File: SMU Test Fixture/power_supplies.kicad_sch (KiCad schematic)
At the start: 60 parts, among them J13 Hot_Spade, J14 Power Outputs, J15 Neutral_Spade, Q1 IRLR6225TRPBF, Q2 NTD3055-150T4G, Q3 MMBT3906, T1 VPP28-1060, U10 LT3045, U11 LT1086-12, U12 LT3094, U13 LTC2966CSWPBF, U9 LT1086-5.0

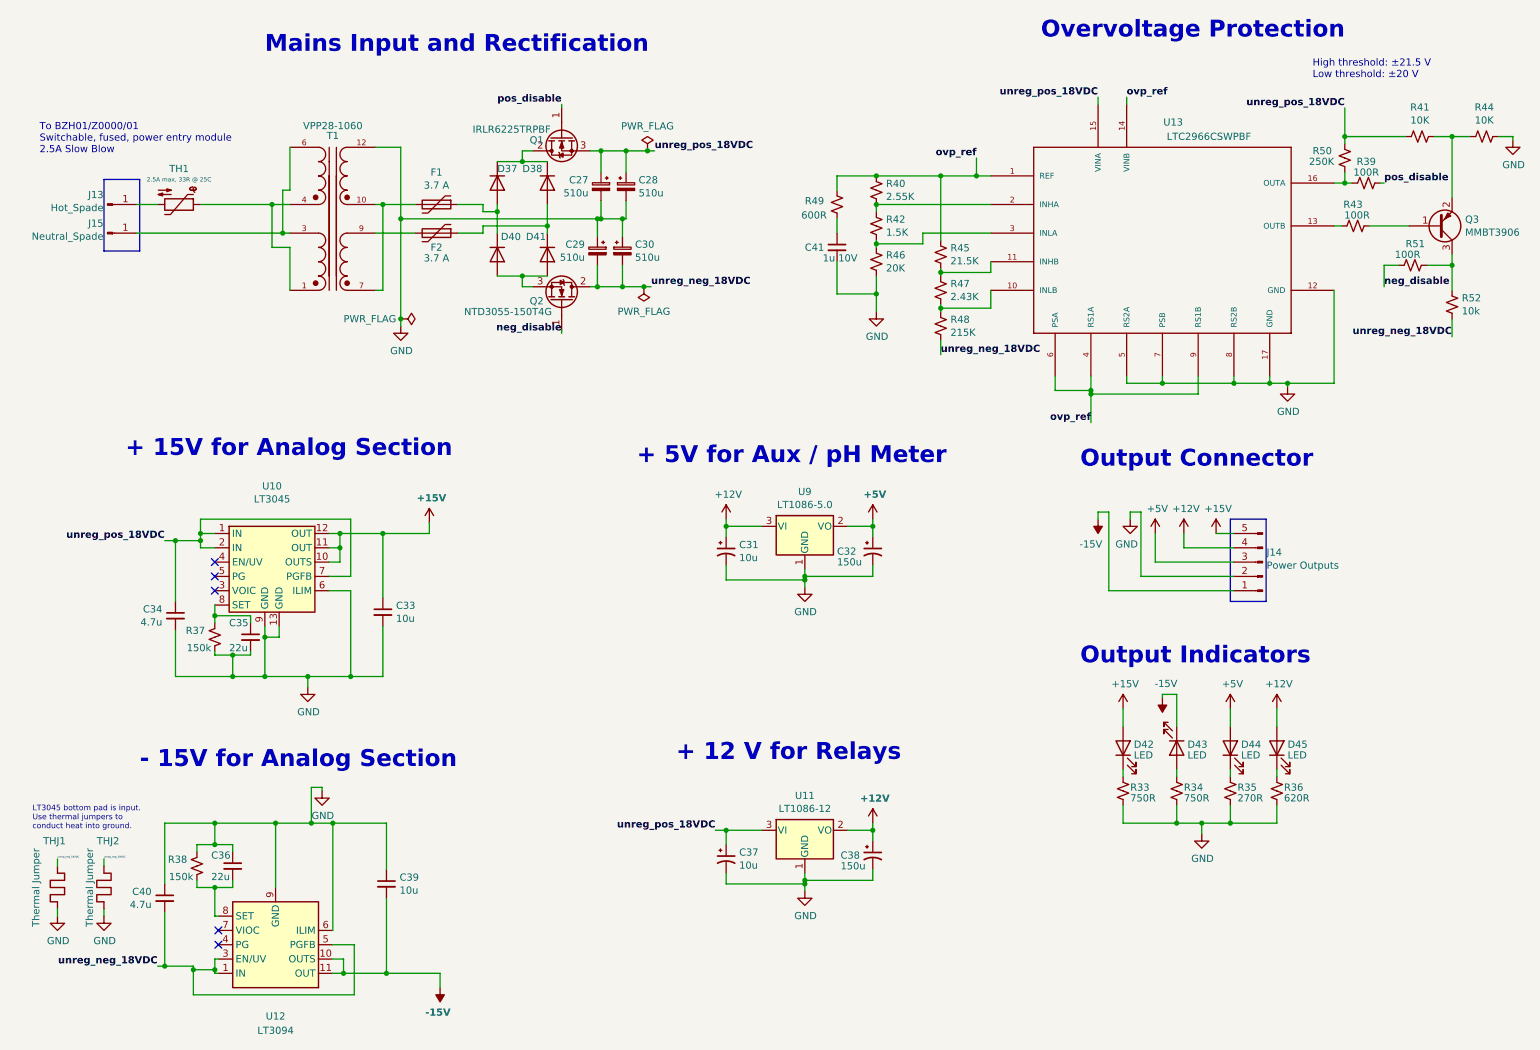
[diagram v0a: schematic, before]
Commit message: Fix grid nightmare. Begin adding bypass caps for a.switches
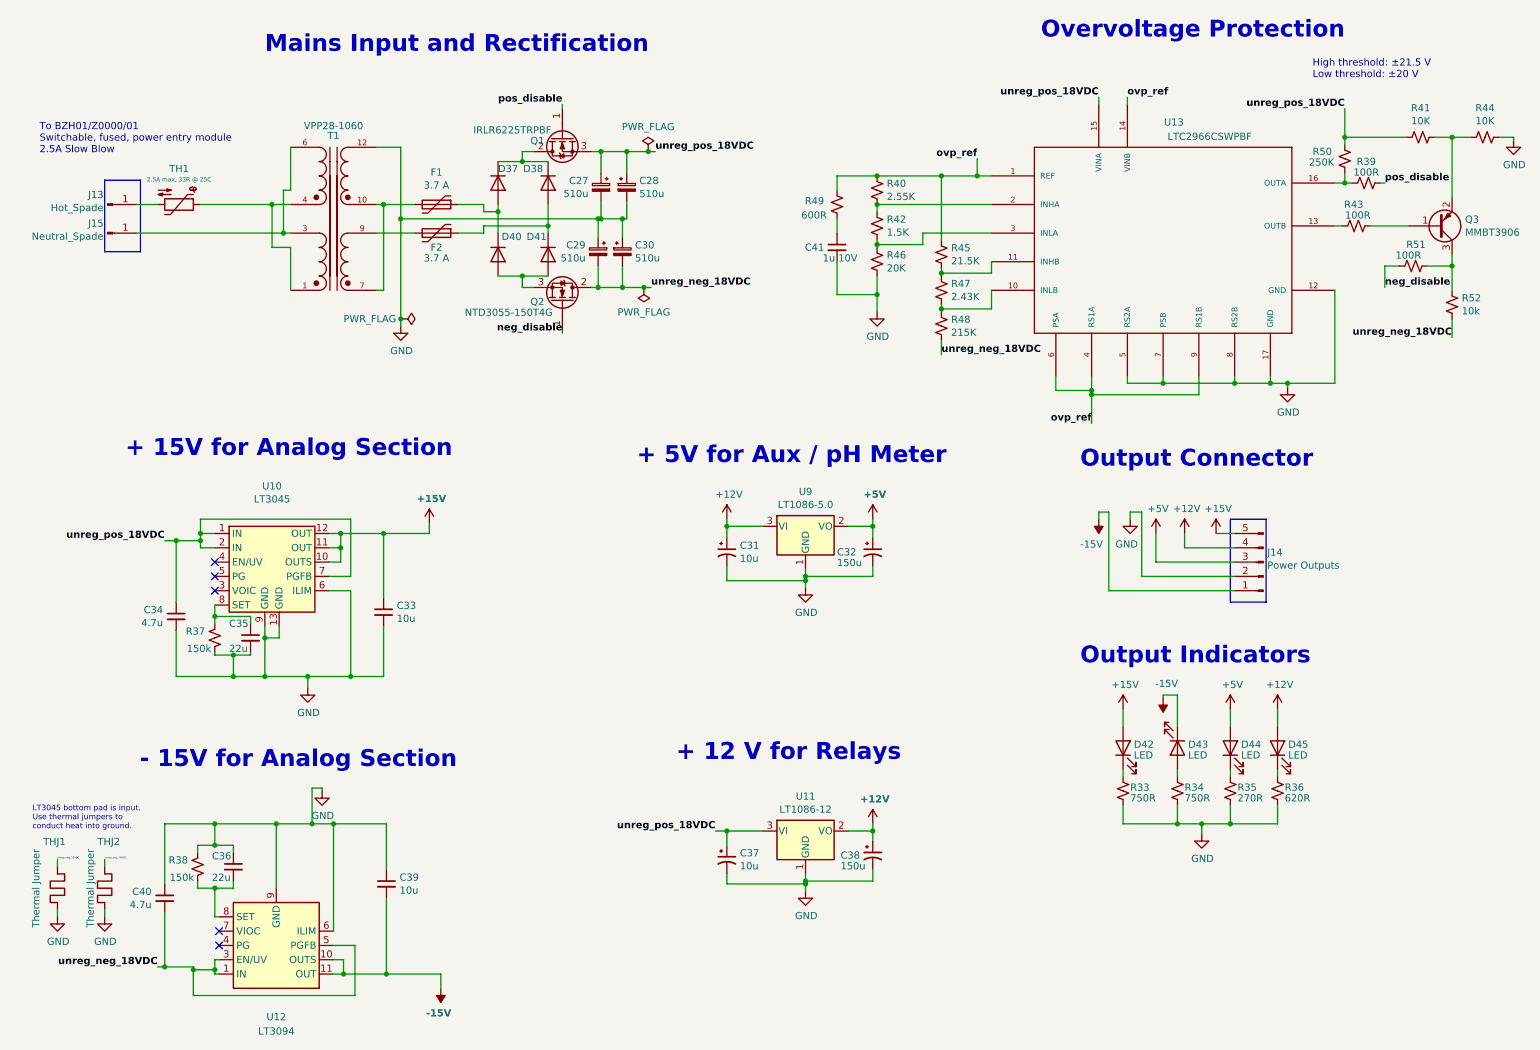
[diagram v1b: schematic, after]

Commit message: Split ADGS1408 units, add switch contorl page
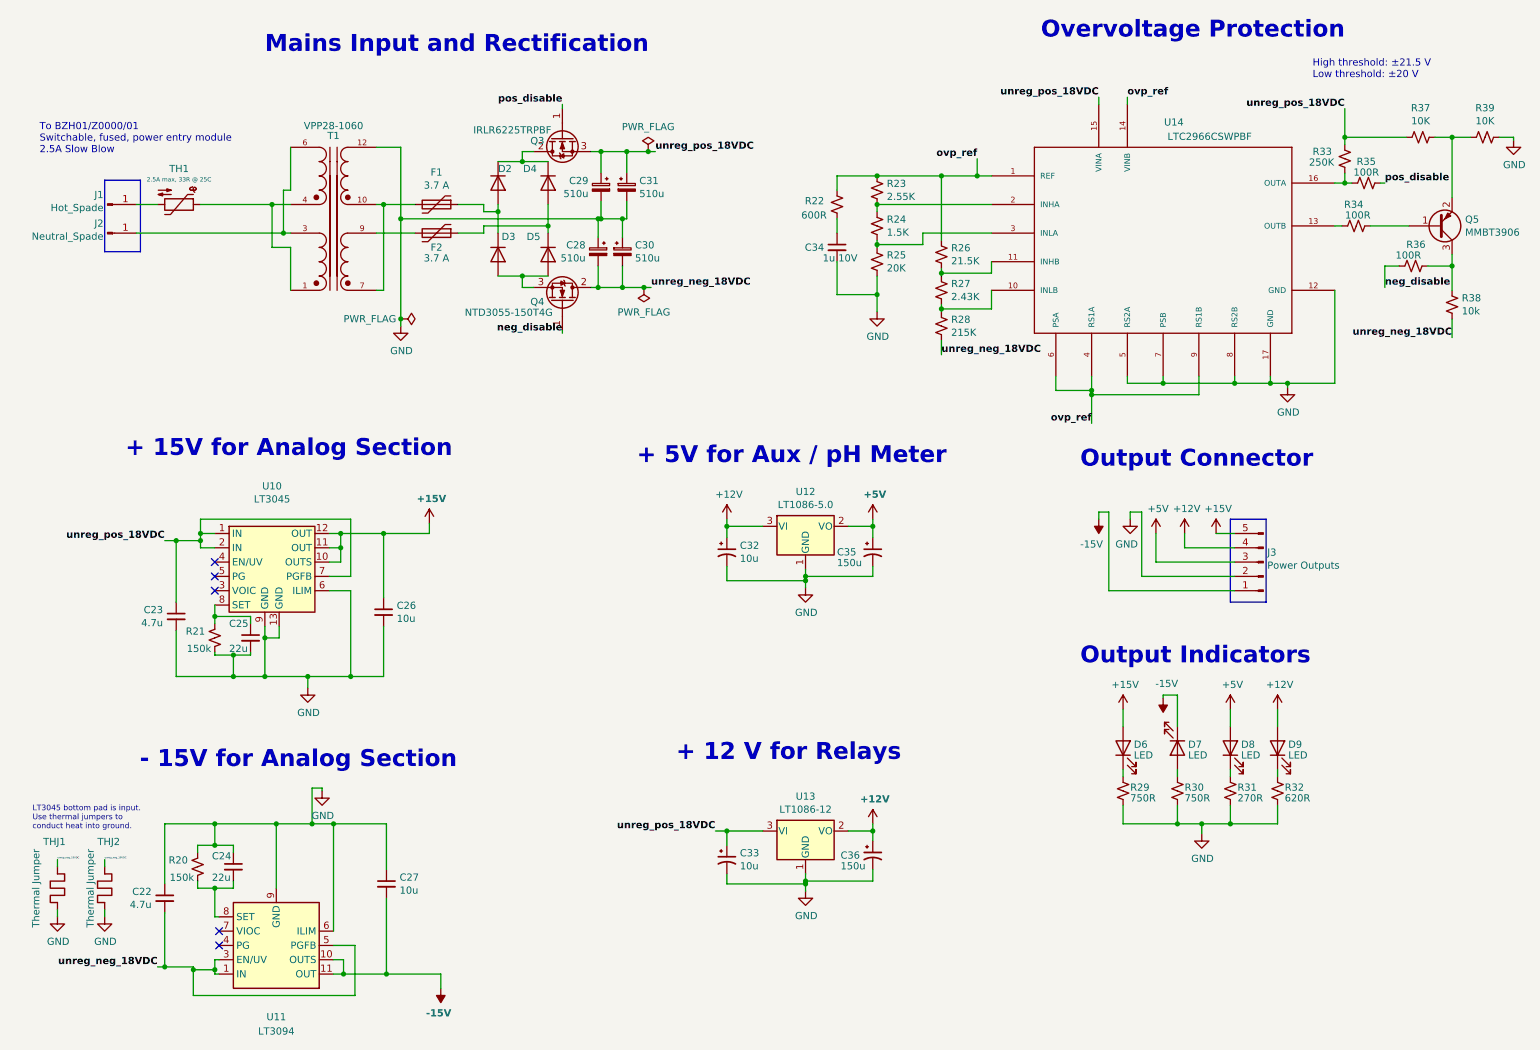
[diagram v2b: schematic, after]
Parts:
- renumbered C40 to C22, C34 to C23, C36 to C24, C35 to C25, C33 to C26, C39 to C27, C29 to C28, C27 to C29, C28 to C31, C31 to C32, C37 to C33, C41 to C34, C32 to C35, C38 to C36, D37 to D2, D40 to D3, D38 to D4, D41 to D5, D42 to D6, D43 to D7, D44 to D8, D45 to D9, J13 to J1, J15 to J2, J14 to J3, Q1 to Q3, Q2 to Q4, Q3 to Q5, R38 to R20, R37 to R21, R49 to R22, R40 to R23, R42 to R24, R46 to R25, R45 to R26, R47 to R27, R48 to R28, R33 to R29, R34 to R30, R35 to R31, R36 to R32, R50 to R33, R43 to R34, R39 to R35, R51 to R36, R41 to R37, R52 to R38, R44 to R39, U12 to U11, U9 to U12, U11 to U13, U13 to U14

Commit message: Symbol fixes, ERC pass
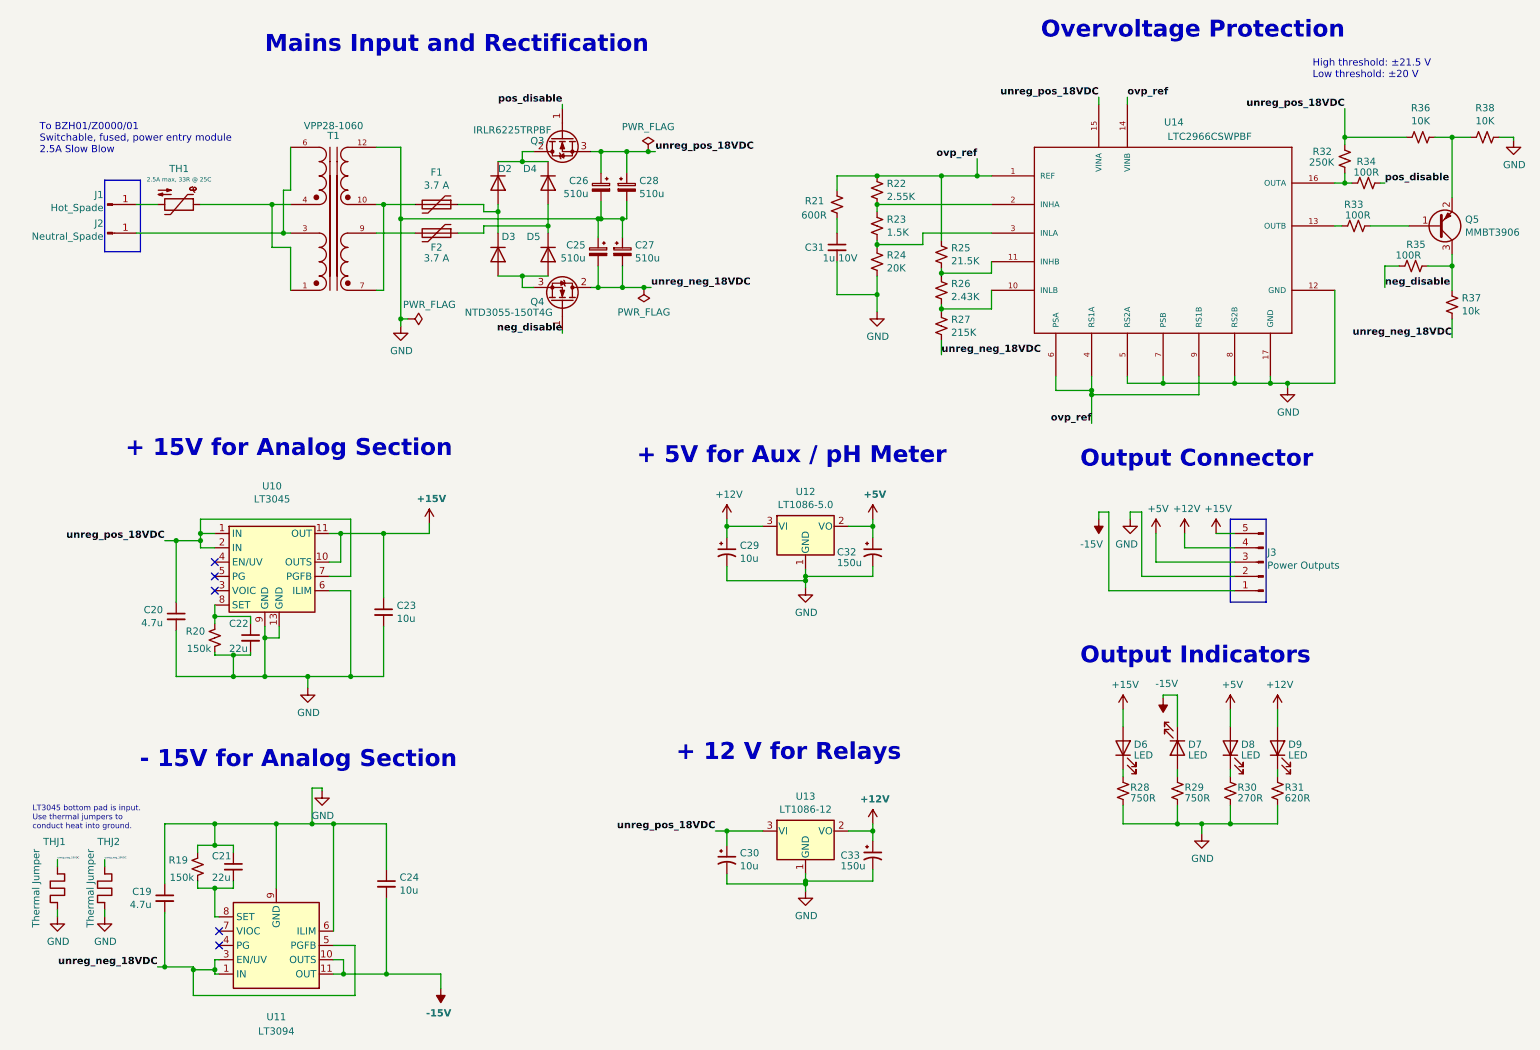
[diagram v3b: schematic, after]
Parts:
- T1: footprint MAGI_Footprints:XFMR_VPP28-1060 -> XFMR_VPP28-1060
- U14: footprint Package_DFN_QFN:QFN-16-1EP_3x3mm_P0.5mm_EP1.45x1.45mm -> QFN-16; MANUFACTURER_PART_NUMBER ltc2966csw#pbf -> ltc2966_qfn
- renumbered C22 to C19, C23 to C20, C24 to C21, C25 to C22, C26 to C23, C27 to C24, C28 to C25, C29 to C26, C30 to C27, C31 to C28, C32 to C29, C33 to C30, C34 to C31, C35 to C32, C36 to C33, R20 to R19, R21 to R20, R22 to R21, R23 to R22, R24 to R23, R25 to R24, R26 to R25, R27 to R26, R28 to R27, R29 to R28, R30 to R29, R31 to R30, R32 to R31, R33 to R32, R34 to R33, R35 to R34, R36 to R35, R37 to R36, R38 to R37, R39 to R38
